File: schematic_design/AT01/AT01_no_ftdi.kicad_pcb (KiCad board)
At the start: 2 copper layers, 70 x 55 mm, 69 parts, among them J1 JST Connector, J2 USB_C_Receptacle_USB2.0, J3 Conn_01x08, J4 Solenoid Valve Connector, J5 DC Pump Connector, J6 PPG Sensor Input, K1 TLP4590ATP1_F, Q2 FDS6375, SW1 SW_Push, SW2 SW_Push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

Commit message: final rev1.0 design
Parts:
- removed D11, D6: PESD3V3S1UB,115, Diode_SMD:D_SOD-523
- removed H4: MountingHole, MountingHole:MountingHole_2.2mm_M2_ISO7380
- added D12: PESD3V3S1UB,115, Diode_SMD:D_SOD-523, F.Cu at (127.6, 98.2)
- added D3: ESD9101P2T5G, Diode_SMD:D_SOD-923, F.Cu at (127.9, 104.4)
- added R2: 0, Resistor_SMD:R_0603_1608Metric_Pad0.98x0.95mm_HandSolder, F.Cu at (133.5, 109.1)
- C7: footprint Capacitor_SMD:C_0603_1608Metric_Pad1.08x0.95mm_HandSolder -> Capacitor_SMD:C_0805_2012Metric_Pad1.18x1.45mm_HandSolder
- D2: value ESD9101P2T5G -> PESD3V3S1UB,115; footprint Diode_SMD:D_SOD-923 -> Diode_SMD:D_SOD-523
- J6: footprint Connector_PinSocket_2.54mm:PinSocket_1x02_P2.54mm_Vertical -> Connector_PinHeader_2.54mm:PinHeader_1x02_P2.54mm_Vertical
- moved D2 3.02 mm to (127.9, 101.4)
- moved L1 1.39 mm to (133.9, 113.7)
- moved R6 0.91 mm to (178.1, 82.9)
- moved C17 0.40 mm to (136.4, 89.9)
- moved C7 0.36 mm to (133.3, 90.1)
- moved R1 0.10 mm to (178.1, 76.1)
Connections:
- D2 pad 1: VBUS -> Net-(D2-K)
- J2 pad A6: Net-(D6A-K1) -> Net-(D2-K)
- J2 pad B6: Net-(D6A-K1) -> Net-(D2-K)
- K1 pad 2: VBUS -> Net-(K1-Pad2)
- U6 pad 14: Net-(D6A-K1) -> Net-(D2-K)
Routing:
- net Net-(D6A-K1): track 20.9 -> 0.00 mm, vias 2 -> 0
- net Net-(D2-K): track 0.00 -> 20.9 mm, vias 0 -> 2
- net Net-(K1-Pad2): track 0.00 -> 14.6 mm, vias 0 -> 2
- net VBUS: track 58.3 -> 44.6 mm, vias 6 -> 4
- net GND: track 58.4 -> 60.3 mm
- net Net-(D7-A): track 35.3 -> 34.2 mm
- net Net-(D12-A): track 21.7 -> 20.8 mm
- net Net-(U6-IO41): track 23.2 -> 22.3 mm

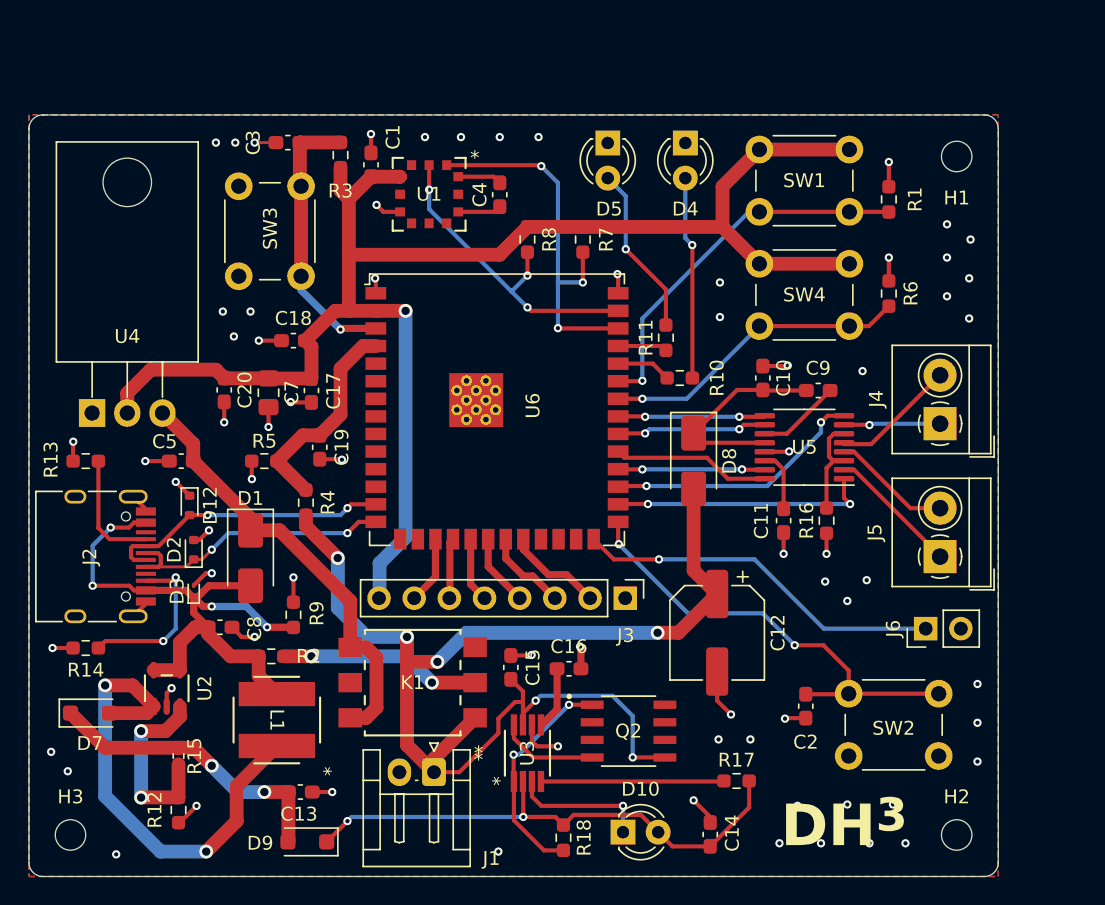
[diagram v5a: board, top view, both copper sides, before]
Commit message: reworking usb c connection
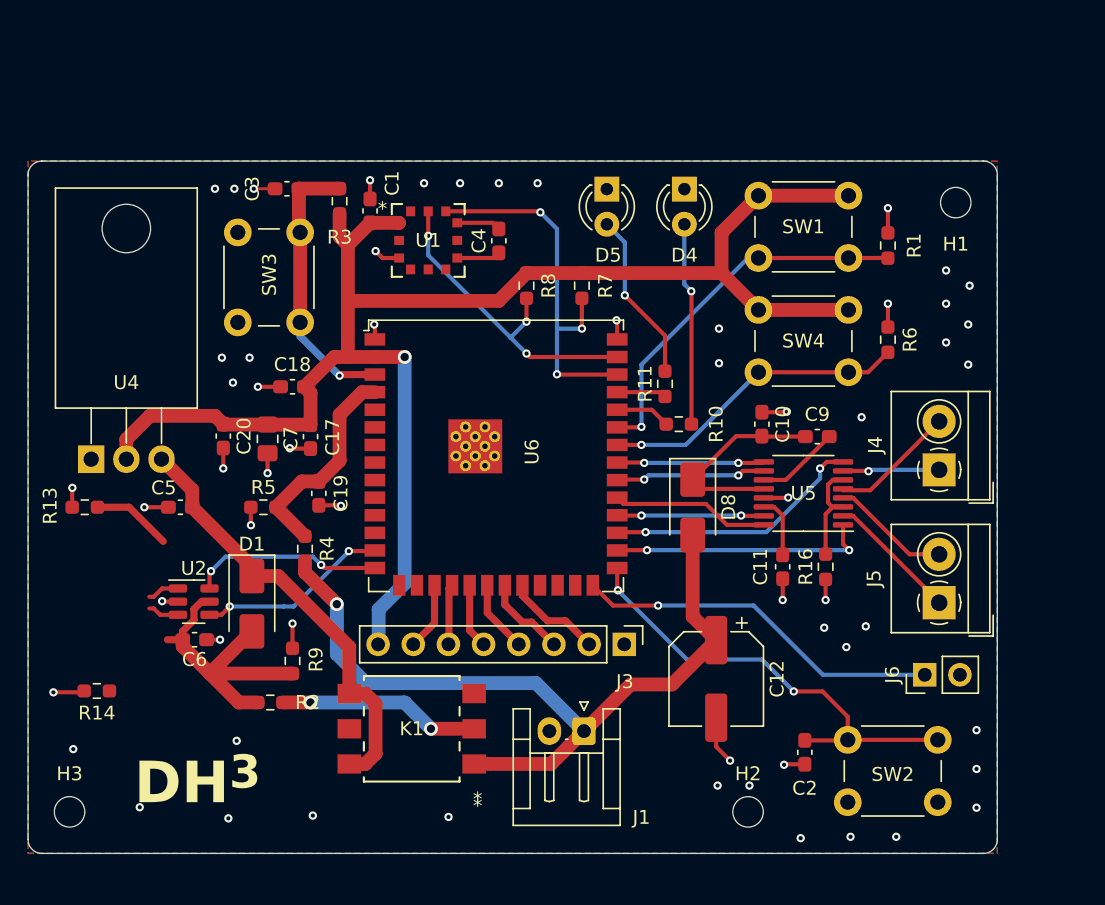
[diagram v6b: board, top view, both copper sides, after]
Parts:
- removed C13, C14, C15: 10uF, Capacitor_SMD:C_0603_1608Metric_Pad1.08x0.95mm_HandSolder
- removed C16: 0.1uF, Capacitor_SMD:C_0603_1608Metric_Pad1.08x0.95mm_HandSolder
- removed C8: 4.7uF, Capacitor_SMD:C_0603_1608Metric_Pad1.08x0.95mm_HandSolder
- removed D10: LED, LED_THT:LED_D3.0mm
- removed D12, D2: PESD3V3S1UB,115, Diode_SMD:D_SOD-523
- removed D3: ESD9101P2T5G, Diode_SMD:D_SOD-923
- removed D7, D9: MBRM120LT3G, Diode_SMD:D_SOD-123F
- removed J2: USB_C_Receptacle_USB2.0, Connector_USB:USB_C_Receptacle_HRO_TYPE-C-31-M-12
- removed L1: 2.7uH, Library:IND_R2NC_SUM
- removed Q2: FDS6375, Library:SOIC127P600X175-8N
- removed R12: 10K, Resistor_SMD:R_0603_1608Metric_Pad0.98x0.95mm_HandSolder
- removed R15: 61.2K, Resistor_SMD:R_0402_1005Metric_Pad0.72x0.64mm_HandSolder
- removed R17: 100K, Resistor_SMD:R_0603_1608Metric_Pad0.98x0.95mm_HandSolder
- removed R18: 220m, Resistor_SMD:R_0603_1608Metric_Pad0.98x0.95mm_HandSolder
- removed U3: MCP73844T-840I/MS, Library:MSOP8_MC_MCH
- added C6: 100nF, Capacitor_SMD:C_0603_1608Metric_Pad1.08x0.95mm_HandSolder, F.Cu at (128.0, 107.9)
- U2: value LT1935ES5-TRPBF -> USBLC6-2SC6; footprint Library:S_5_ADI -> Package_TO_SOT_SMD:SOT-23-6
- moved H2 15.2 mm to (167.9, 120.3)
- moved J1 11.2 mm to (156.1, 114.5)
- moved U2 6.56 mm to (127.9, 105.2), turned to 0 degrees
- moved C1 3.33 mm to (140.6, 76.9)
- moved J6 3.33 mm to (180.7, 110.4)
- moved R1 3.33 mm to (178.0, 79.4)
- moved R2 3.33 mm to (133.4, 112.4)
- moved R9 3.33 mm to (135.0, 109.4)
- moved C7 3.33 mm to (133.2, 93.4)
- moved D5 3.33 mm to (157.7, 75.4)
- moved J4 3.33 mm to (181.7, 95.6)
- moved J5 3.33 mm to (181.7, 105.2)
- moved U6 3.33 mm to (149.7, 94.6)
- moved C10 3.33 mm to (168.9, 92.3)
- moved C11 3.33 mm to (170.4, 102.6)
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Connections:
- U2 pad 1: Net-(D7-A) -> /D+
- U2 pad 3: Net-(U2-FB) -> /D-
- U2 pad 4: VBUS -> Net-(U6-IO19)
- U6 pad 13: Net-(D12-A) -> Net-(U6-IO19)
- U6 pad 14: Net-(D2-K) -> Net-(U6-IO20)
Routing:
- net Net-(D10-A): track 38.4 -> 0.00 mm, vias 2 -> 0
- net Net-(D7-A): track 34.2 -> 0.00 mm, vias 2 -> 0
- net VBAT: track 90.0 -> 57.3 mm, vias 6 -> 1
- net VBUS: track 44.6 -> 22.8 mm, vias 4 -> 0
- net Net-(D7-K): track 21.7 -> 0.00 mm, vias 2 -> 0
- net Net-(D2-K): track 20.9 -> 0.00 mm, vias 2 -> 0
- net Net-(D12-A): track 20.8 -> 0.00 mm, vias 2 -> 0
- net GND: track 60.3 -> 40.3 mm, vias 71 -> 60
- net Net-(U3-SENSE): track 16.4 -> 0.00 mm, vias 2 -> 0
- net Net-(U6-IO20): track 0.00 -> 13.9 mm, vias 0 -> 2
- net Net-(U6-IO19): track 0.00 -> 13.9 mm, vias 0 -> 2
- net Net-(U2-FB): track 13.9 -> 0.00 mm, vias 2 -> 0
- net Net-(U3-EN): track 13.2 -> 0.00 mm
- net Net-(J2-CC2): track 12.1 -> 0.02 mm, vias 2 -> 0
- net Net-(D10-K): track 9.84 -> 0.00 mm, vias 1 -> 0
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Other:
- board size 70 x 55 mm -> 70 x 50 mm

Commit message: updating load sharing circuit
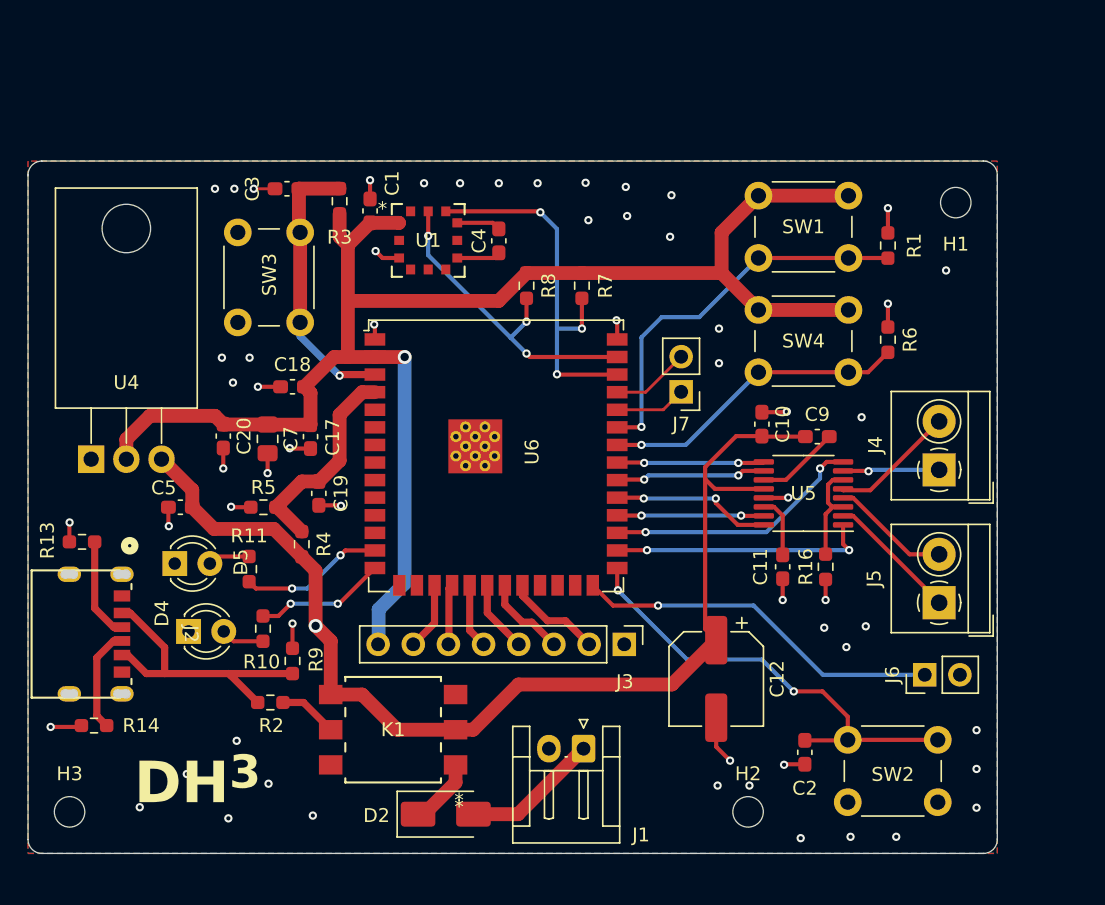
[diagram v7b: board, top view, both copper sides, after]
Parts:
- removed C6: 100nF, Capacitor_SMD:C_0603_1608Metric_Pad1.08x0.95mm_HandSolder
- removed D1, D8: B120-E3, Diode_SMD:D_SMA
- removed U2: USBLC6-2SC6, Package_TO_SOT_SMD:SOT-23-6
- added D2: B120-E3, Diode_SMD:D_SMA, F.Cu at (146.1, 120.5)
- added J2: USB4125-GF-A-0190, Library:CONN6_125-GF-A-0190_GCT, F.Cu at (122.7, 104.7)
- added J7: RX/TX Breakout, Connector_PinHeader_2.54mm:PinHeader_1x02_P2.54mm_Vertical, F.Cu at (163.1, 90.0)
- moved D4 48.0 mm to (127.5, 107.3), turned to 0 degrees
- moved D5 41.3 mm to (126.5, 102.4), turned to 0 degrees
- moved R10 33.5 mm to (132.9, 107.1), turned to 90 degrees
- moved R11 32.9 mm to (131.9, 102.8)
- moved R13 2.51 mm to (119.8, 100.8)
- moved R14 2.51 mm to (120.7, 114.1)
- moved K1 1.34 mm to (142.3, 114.4)
- moved J1 1.27 mm to (156.1, 115.8)
- moved R4 0.41 mm to (135.7, 101.0)
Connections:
- C10 pad 2: Net-(D8-K) -> VCC
- C12 pad 1: VBAT -> VCC
- C5 pad 1: Net-(D1-K) -> VCC
- C9 pad 2: Net-(D8-K) -> VCC
- J1 pad 1: VBAT -> Net-(D2-A)
- K1 pad 1: VBAT -> Net-(D2-K)
- K1 pad 2: Net-(K1-Pad2) -> VCC
- K1 pad 4: Net-(D1-K) -> VCC
- K1 pad 5: unconnected-(K1-Pad5) -> Net-(K1-Pad5)
- K1 pad 6: Net-(D1-K) -> unconnected-(K1-Pad6)
- R10 pad 2: Net-(U6-RXD0) -> Net-(U6-IO20)
- R11 pad 1: Net-(U6-TXD0) -> Net-(U6-IO19)
- R2 pad 2: Net-(K1-Pad2) -> Net-(K1-Pad5)
- R4 pad 2: VBAT -> VCC
- U4 pad 3: Net-(D1-K) -> VCC
- U5 pad 12: Net-(D8-K) -> VCC
- U6 pad 36: Net-(U6-RXD0) -> Net-(J7-Pin_1)
- U6 pad 37: Net-(U6-TXD0) -> Net-(J7-Pin_2)
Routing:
- net VCC: track 0.00 -> 82.6 mm, vias 0 -> 1
- net VBAT: track 57.3 -> 0.00 mm, vias 1 -> 0
- net Net-(D1-K): track 31.7 -> 0.00 mm
- net Net-(D8-K): track 14.9 -> 0.00 mm
- net Net-(K1-Pad2): track 14.6 -> 0.00 mm, vias 2 -> 0
- net Net-(D4-A): track 14.6 -> 3.13 mm, vias 1 -> 0
- net Net-(D2-A): track 0.00 -> 9.91 mm
- net Net-(D5-A): track 12.3 -> 3.05 mm, vias 1 -> 0
- net Net-(J2-CC2): track 0.02 -> 7.51 mm
- net Net-(J7-Pin_2): track 0.00 -> 5.68 mm
- net Net-(J7-Pin_1): track 0.00 -> 5.15 mm
- net Net-(D2-K): track 0.00 -> 4.93 mm
- net Net-(U6-IO20): track 13.9 -> 9.52 mm
- net Net-(K1-Pad5): track 0.00 -> 4.17 mm
- net Net-(U6-RXD0): track 3.97 -> 0.00 mm
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
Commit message: Rev3.0 board commits
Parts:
- J2: value USB4125-GF-A-0190 -> USB4125-GF-A-0190_REVA2; footprint Library:CONN6_125-GF-A-0190_GCT -> Library:GCT_USB4125-GF-A-0190_REVA2
- moved J2 4.02 mm to (119.7, 107.4)
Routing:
- net GND: track 37.9 -> 41.1 mm
- net VCC: track 82.6 -> 81.7 mm, vias 1 -> 0
- net VBUS: track 21.9 -> 21.1 mm
